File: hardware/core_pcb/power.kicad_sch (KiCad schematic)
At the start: 36 parts, among them J1 24VDC IN, U1 TPS54360DDA, U2 TLV62569DBV

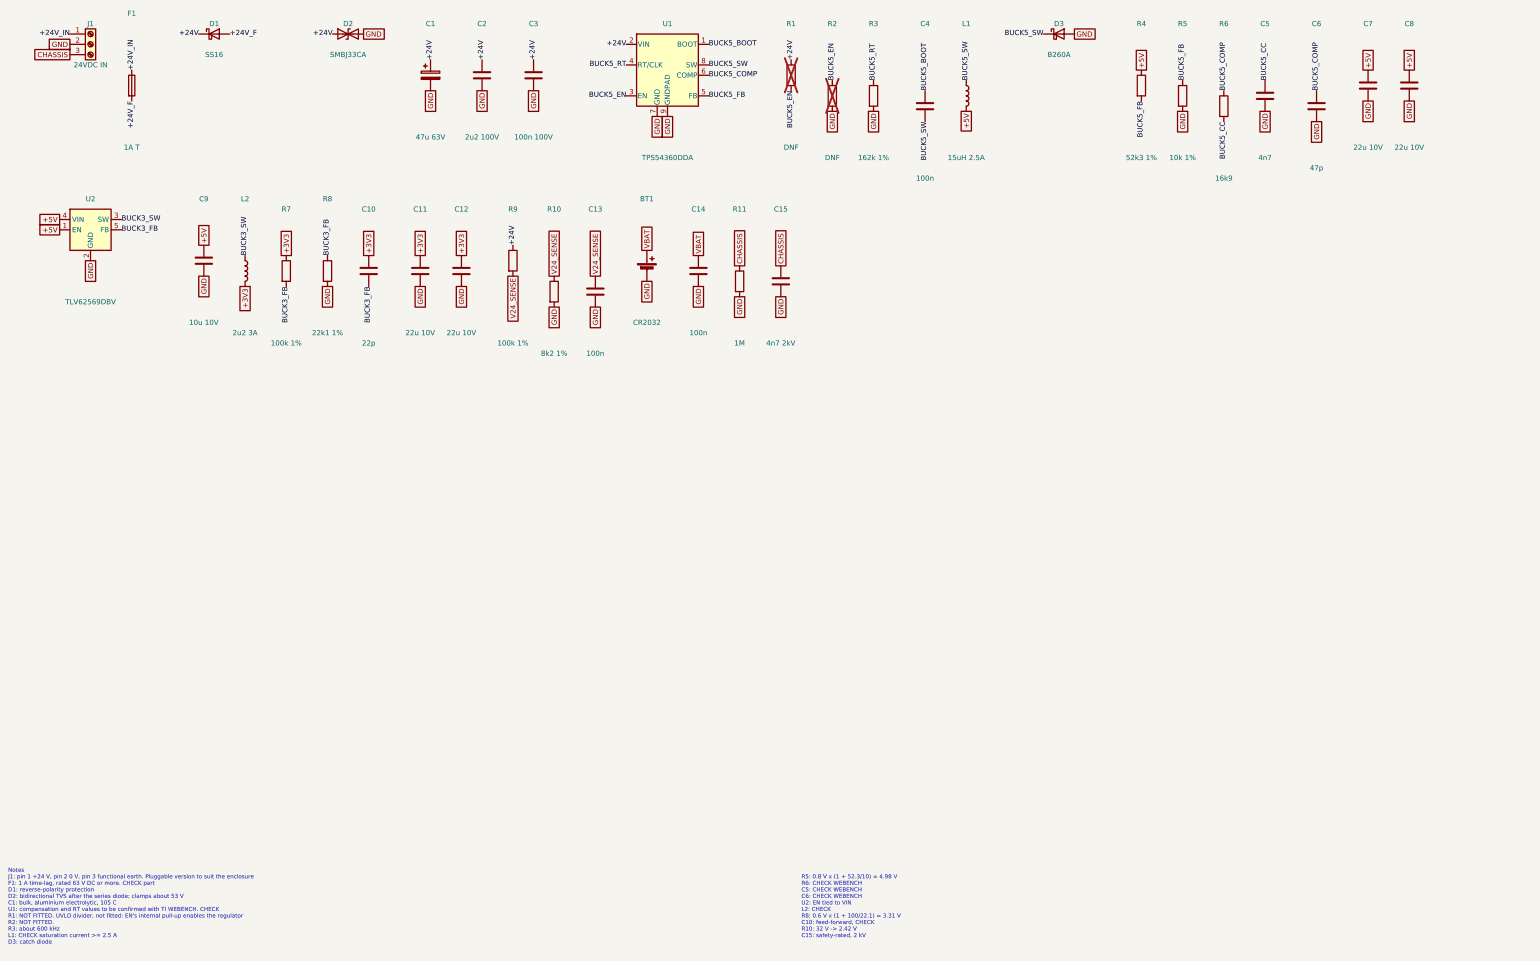
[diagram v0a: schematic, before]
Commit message: Core PCB: close the platform spec's gaps (CIP-01.3, 07.3, 24, 04.4/20.4)
- CORE_PCB.md 12: hardware revision strap encoding (PE7/PE8) and 24 V sense scaling (PC0)
- CORE_PCB.md 13: debug lock (Closed with debug authentication) and SWD recovery route
- CORE_PCB_EMC.md: IEC 61326-1 industrial immunity levels, CISPR 11 class A, environment, IP
- Schematic: 24 V input gets a common-mode choke (L3), Y-capacitors (C16, C17) and a 3 kW
  TVS (SMDJ33CA) for the IEC 61000-4-4/-5 levels; netlist check passes (148 parts)

Co-Authored-By: Claude Opus 5.5 (1M context) <noreply@anthropic.com>
Claude-Session: https://claude.ai/code/session_014onnq3eRiDkqdAB6fKiRDW
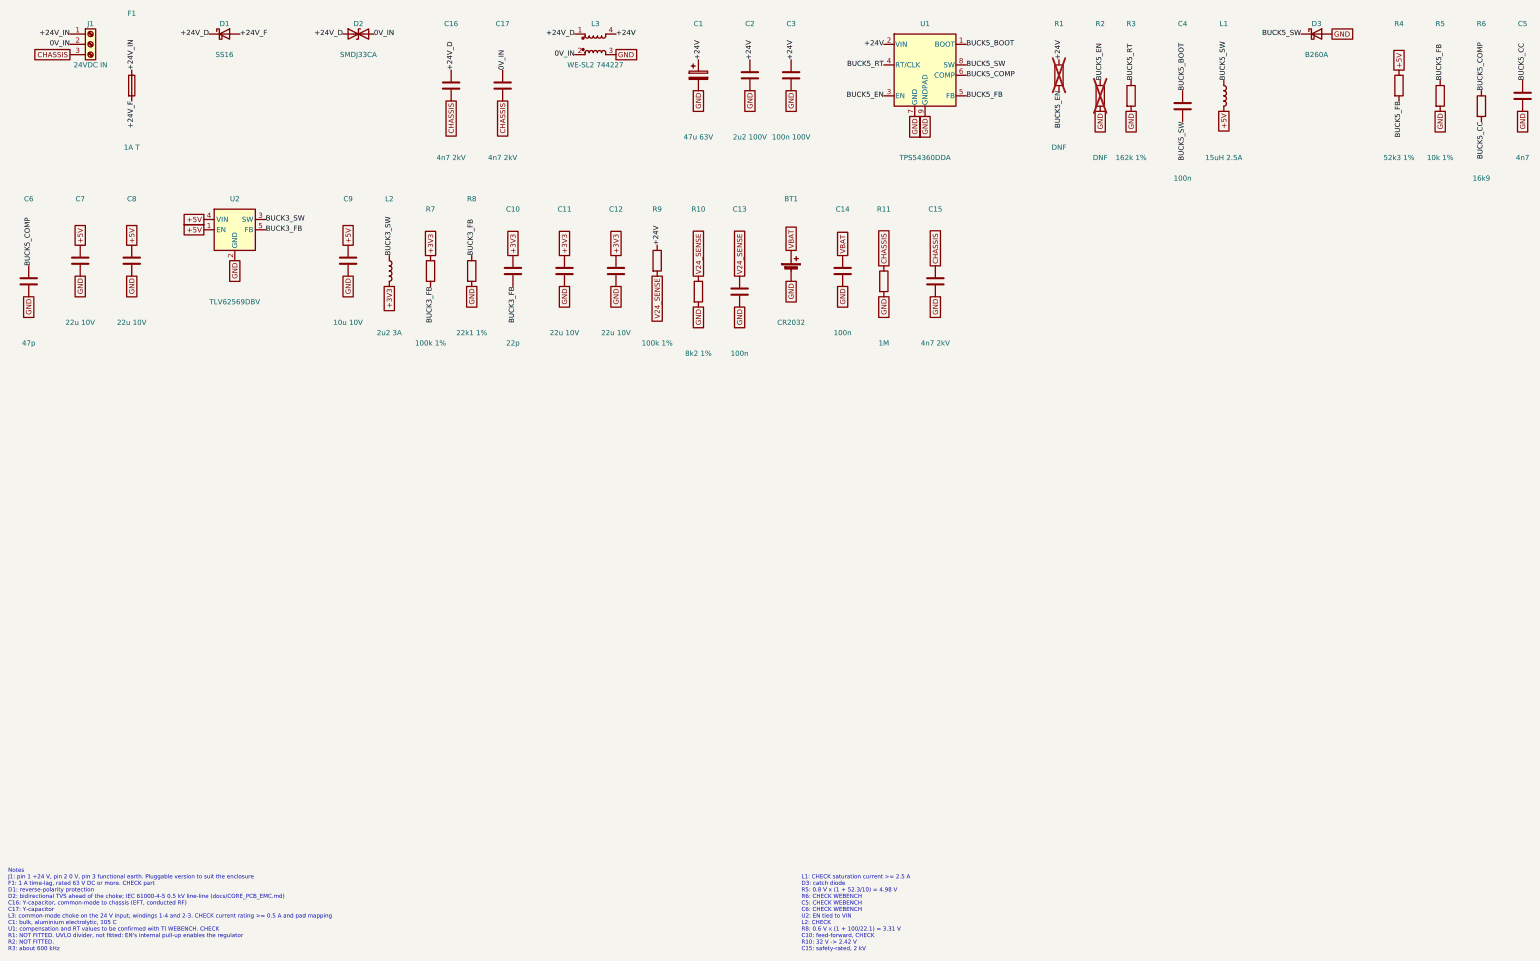
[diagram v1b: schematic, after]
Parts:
- added C16, C17: 4n7 2kV, Capacitor_SMD:C_1812_4532Metric, symbol Device:C
- added L3: WE-SL2 744227, Inductor_SMD:L_CommonMode_Wuerth_WE-SL2, symbol Device:L_Coupled_1423
- D2: value SMBJ33CA -> SMDJ33CA; footprint Diode_SMD:D_SMB -> Diode_SMD:D_SMC; MPN SMBJ33CA -> SMDJ33CA (3 kW)
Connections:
- net +24V: now also L3.4; no longer D1.1 (K), D2.1 (A1)
- net CHASSIS: now also C16.2, C17.2
- net GND: now also L3.3; no longer D2.2 (A2), J1.2 (Pin_2)
- new net +24V_D: C16.1, D1.1 (K), D2.1 (A1), L3.1
- new net 0V_IN: C17.1, D2.2 (A2), J1.2 (Pin_2), L3.2
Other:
- note added: "L1: CHECK saturation current >= 2.5 A D3: catch diode R5: 0.8 V x (1 + 52.3/10) = 4.98 V R6: CHECK WEBENCH C5: CHECK WEBENCH C6: CHECK WEBENCH U2: EN tied to VIN L2: CHECK R8: 0.6 V x (1 + 100/22.1) = 3.31 V C10: feed-forward, CHECK R10: 32 V -> 2.42 V C15: safety-rated, 2 kV"
- note added: "Notes J1: pin 1 +24 V, pin 2 0 V, pin 3 functional earth. Pluggable version to suit the enclosure F1: 1 A time-lag, rated 63 V DC or more. CHECK part D1: reverse-polarity protection D2: bidirectional TVS ahead of the choke; IEC 61000-4-5 0.5 kV line-line (docs/CORE_PCB_EMC.md) C16: Y-capacitor, common-mode to chassis (EFT, conducted RF) C17: Y-capacitor L3: common-mode choke on the 24 V input; wi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"
- note removed: "Notes J1: pin 1 +24 V, pin 2 0 V, pin 3 functional earth. Pluggable version to suit the enclosure F1: 1 A time-lag, rated 63 V DC or more. CHECK part D1: reverse-polarity protection D2: bidirectional TVS after the series diode; clamps about 53 V C1: bulk, aluminium electrolytic, 105 C U1: compensation and RT values to be confirmed with TI WEBENCH. CHECK R1: NOT FITTED. UVLO divider, not fitted: E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"
- note removed: "R5: 0.8 V x (1 + 52.3/10) = 4.98 V R6: CHECK WEBENCH C5: CHECK WEBENCH C6: CHECK WEBENCH U2: EN tied to VIN L2: CHECK R8: 0.6 V x (1 + 100/22.1) = 3.31 V C10: feed-forward, CHECK R10: 32 V -> 2.42 V C15: safety-rated, 2 kV"
- moved on the sheet: BT1, C1, C10, C11, C12, C13, C14, C15, C2, C3, C4, C5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

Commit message: Core PCB: 24 V hold-up (2 x 470 uF 63 V) for the firmware's 20 ms power-fail window; fuse to 2 A T
Co-Authored-By: Claude Opus 5.5 (1M context) <noreply@anthropic.com>
Claude-Session: https://claude.ai/code/session_014onnq3eRiDkqdAB6fKiRDW
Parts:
- added C18, C19: 470u 63V, Capacitor_THT:CP_Radial_D12.5mm_P5.00mm, symbol Device:C_Polarized
- F1: value 1A T -> 2A T; MPN 1A T -> 2A T
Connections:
- net +24V: now also C18.1, C19.1
- net GND: now also C18.2, C19.2
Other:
- note added: "Notes J1: pin 1 +24 V, pin 2 0 V, pin 3 functional earth. Pluggable version to suit the enclosure F1: 2 A time-lag, rated 63 V DC or more, I2t for the hold-up capacitors' inrush. CHECK part D1: reverse-polarity protection D2: bidirectional TVS ahead of the choke; IEC 61000-4-5 0.5 kV line-line (docs/CORE_PCB_EMC.md) C16: Y-capacitor, common-mode to chassis (EFT, conducted RF) C17: Y-capacitor L3: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"
- note removed: "Notes J1: pin 1 +24 V, pin 2 0 V, pin 3 functional earth. Pluggable version to suit the enclosure F1: 1 A time-lag, rated 63 V DC or more. CHECK part D1: reverse-polarity protection D2: bidirectional TVS ahead of the choke; IEC 61000-4-5 0.5 kV line-line (docs/CORE_PCB_EMC.md) C16: Y-capacitor, common-mode to chassis (EFT, conducted RF) C17: Y-capacitor L3: common-mode choke on the 24 V input; wi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"
- moved on the sheet: BT1, C10, C11, C12, C13, C14, C15, C2, C3, C4, C5, C6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

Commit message: Core PCB: save datasheets and clear the datasheet checks
Add hardware/datasheets with the six datasheets Gary supplied and an index.
Apply what they show: TPS54360B with 22 uH and compensation from its
datasheet, LAN8742A crystal caps 33 pF, W5500 reserved pins 38-42 left open
and its reference crystal circuit (1M, 0R), FRAM and choke checks cleared.

Co-Authored-By: Claude Opus 5.5 (1M context) <noreply@anthropic.com>
Claude-Session: https://claude.ai/code/session_014onnq3eRiDkqdAB6fKiRDW
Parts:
- C5: value 4n7 -> 33n; MPN 4n7 -> 33n
- C6: value 47p -> 100p; MPN 47p -> 100p
- L1: value 15uH 2.5A -> 22uH; MPN Bourns SRN6045TA-150M -> Bourns SRN6045TA-220M
- R6: value 16k9 -> 4k99 1%; MPN 16k9 -> 4k99 1%
- U1: value TPS54360DDA -> TPS54360B; MPN TPS54360DDAR -> TPS54360BDDAR
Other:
- note added: "R3: about 600 kHz L1: 22 uH for 30 % ripple at 1 A, 600 kHz, 24 V in. CHECK Isat >= 1.6 A D3: catch diode R5: 0.8 V x (1 + 52.3/10) = 4.98 V R6: type II compensation, crossover about 18 kHz U2: EN tied to VIN L2: CHECK R8: 0.6 V x (1 + 100/22.1) = 3.31 V C10: feed-forward, CHECK R10: 32 V -> 2.42 V C15: safety-rated, 2 kV"
- note removed: "L1: CHECK saturation current >= 2.5 A D3: catch diode R5: 0.8 V x (1 + 52.3/10) = 4.98 V R6: CHECK WEBENCH C5: CHECK WEBENCH C6: CHECK WEBENCH U2: EN tied to VIN L2: CHECK R8: 0.6 V x (1 + 100/22.1) = 3.31 V C10: feed-forward, CHECK R10: 32 V -> 2.42 V C15: safety-rated, 2 kV"
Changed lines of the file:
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@@
     (comment 2 "Generated from design.py")
   )
-  (text "Notes\nJ1: pin 1 +24 V, pin 2 0 V, pin 3 functional earth. Pluggable version to suit the enclosure\nF1: 2 A time-lag, rated 63 V DC or more, I2t for the hold-up capacitors' inrush. CHECK part\nD1: reverse-polarity protection\nD2: bidirectional TVS ahead of the choke; IEC 61000-4-5 0.5 kV line-line (docs/CORE_PCB_EMC.md)\nC16: Y-capacitor, common-mode to chassis (EFT, conducted RF)\nC17: Y-capacitor\nL3: common-mode choke on the 24 V input; windings 1-4 and 2-3. CHECK current rating >= 0.5 A and pad mapping\nC1: bulk, aluminium electrolytic, 105 C\nC18: hold-up with C19: 16 V to 6 V gives 20 ms at full load, 40 ms with the backlight off (CORE_PCB.md 5a)\nU1: compensation and RT values to be confirmed with TI WEBENCH. CHECK\nR1: NOT FITTED. UVLO divider, not fitted: EN's internal pull-up enables the regulator\nR2: NOT FITTED.\nR3: about 600 kHz"
+  (text "Notes\nJ1: pin 1 +24 V, pin 2 0 V, pin 3 functional earth. Pluggable version to suit the enclosure\nF1: 2 A time-lag, rated 63 V DC or more, I2t for the hold-up capacitors' inrush. CHECK part\nD1: reverse-polarity protection\nD2: bidirectional TVS ahead of the choke; IEC 61000-4-5 0.5 kV line-line (docs/CORE_PCB_EMC.md)\nC16: Y-capacitor, common-mode to chassis (EFT, conducted RF)\nC17: Y-capacitor\nL3: common-mode choke on the 24 V input; windings 1-4 and 2-3 (datasheet: 1 A, 80 V, 0.16 R; footprint pads match)\nC1: bulk, aluminium electrolytic, 105 C\nC18: hold-up with C19: 16 V to 6 V gives 20 ms at full load, 40 ms with the backlight off (CORE_PCB.md 5a)\nU1: TPS54360B, same pinout as TPS54360; RT and compensation from its datasheet eq. 44-51 (CORE_PCB.md 5)\nR1: NOT FITTED. UVLO divider, not fitted: EN's internal pull-up enables the regulator\nR2: NOT FITTED."
     (at 15.24 226.06 0)
     (effects (font (size 1.0 1.0)) (justify left top))
   )
-  (text "\nL1: CHECK saturation current >= 2.5 A\nD3: catch diode\nR5: 0.8 V x (1 + 52.3/10) = 4.98 V\nR6: CHECK WEBENCH\nC5: CHECK WEBENCH\nC6: CHECK WEBENCH\nU2: EN tied to VIN\nL2: CHECK\nR8: 0.6 V x (1 + 100/22.1) = 3.31 V\nC10: feed-forward, CHECK\nR10: 32 V -> 2.42 V\nC15: safety-rated, 2 kV"
+  (text "\nR3: about 600 kHz\nL1: 22 uH for 30 % ripple at 1 A, 600 kHz, 24 V in. CHECK Isat >= 1.6 A\nD3: catch diode\nR5: 0.8 V x (1 + 52.3/10) = 4.98 V\nR6: type II compensation, crossover about 18 kHz\nU2: EN tied to VIN\nL2: CHECK\nR8: 0.6 V x (1 + 100/22.1) = 3.31 V\nC10: feed-forward, CHECK\nR10: 32 V -> 2.42 V\nC15: safety-rated, 2 kV"
     (at 210.82 226.06 0)
     (effects (font (size 1.0 1.0)) (justify left top))
@@
       (effects (font (size 1.27 1.27)))
     )
-    (property "Value" "TPS54360DDA" (id 1) (at 266.7 50.8 0)
+    (property "Value" "TPS54360B" (id 1) (at 266.7 50.8 0)
       (effects (font (size 1.27 1.27)))
     )
@@
       (effects (font (size 1.27 1.27)) hide)
     )
-    (property "MPN" "TPS54360DDAR" (id 4) (at 266.7 27.94 0)
+    (property "MPN" "TPS54360BDDAR" (id 4) (at 266.7 27.94 0)
       (effects (font (size 1.27 1.27)) hide)
     )
@@
       (effects (font (size 1.27 1.27)))
     )
-    (property "Value" "15uH 2.5A" (id 1) (at 340.36 50.8 0)
+    (property "Value" "22uH" (id 1) (at 340.36 50.8 0)
       (effects (font (size 1.27 1.27)))
     )
@@
       (effects (font (size 1.27 1.27)) hide)
     )
-    (property "MPN" "Bourns SRN6045TA-150M" (id 4) (at 340.36 35.56 0)
+    (property "MPN" "Bourns SRN6045TA-220M" (id 4) (at 340.36 35.56 0)
       (effects (font (size 1.27 1.27)) hide)
     )
@@
       (effects (font (size 1.27 1.27)))
     )
-    (property "Value" "16k9" (id 1) (at 20.32 99.06 0)
+    (property "Value" "4k99 1%" (id 1) (at 20.32 99.06 0)
       (effects (font (size 1.27 1.27)))
     )
@@
       (effects (font (size 1.27 1.27)) hide)
     )
-    (property "MPN" "16k9" (id 4) (at 20.32 81.28 0)
+    (property "MPN" "4k99 1%" (id 4) (at 20.32 81.28 0)
       (effects (font (size 1.27 1.27)) hide)
     )
@@
       (effects (font (size 1.27 1.27)))
     )
-    (property "Value" "4n7" (id 1) (at 30.48 93.98 0)
+    (property "Value" "33n" (id 1) (at 30.48 93.98 0)
       (effects (font (size 1.27 1.27)))
     )
@@
       (effects (font (size 1.27 1.27)) hide)
     )
-    (property "MPN" "4n7" (id 4) (at 30.48 78.74 0)
+    (property "MPN" "33n" (id 4) (at 30.48 78.74 0)
       (effects (font (size 1.27 1.27)) hide)
     )
@@
       (effects (font (size 1.27 1.27)))
     )
-    (property "Value" "47p" (id 1) (at 43.18 96.52 0)
+    (property "Value" "100p" (id 1) (at 43.18 96.52 0)
       (effects (font (size 1.27 1.27)))
     )
@@
       (effects (font (size 1.27 1.27)) hide)
     )
-    (property "MPN" "47p" (id 4) (at 43.18 81.28 0)
-      (effects (font (size 1.27 1.27)) hide)
-    )
+    (property "MPN" "100p" (id 4) (at 43.18 81.28 0)
+      (effects (font (size 1.27 1.27)) hide)
+    )

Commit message: CORE PCB rev 0.2: I/O node section on the same board
Three new sheets: field digital I/O with the hardware output gate (ISO2H823V2.5,
ISO808A-1, ISO1I813T), field power / pump / relay coils / USB-C, and the isolated
analog (AD4112) and temperature (ADS124S08) islands. Project symbols for the six
I/O chips missing from KiCad. SPI4 nets renamed: the bus is shared with the I/O chips.
423 parts, netlist check passes. CORE_PCB.md: pin map, connectors, BOM, section 14.

Co-Authored-By: Claude Opus 5.5 <noreply@anthropic.com>
Claude-Session: https://claude.ai/code/session_014onnq3eRiDkqdAB6fKiRDW
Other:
- moved on the sheet: C1, C18, C19, C2, C3, R1, R2, R3, R4, R9
